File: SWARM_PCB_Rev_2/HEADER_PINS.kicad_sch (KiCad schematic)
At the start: 4 parts, among them J3 Conn_02x25_Odd_Even, J4 Conn_02x25_Odd_Even, J5 Conn_02x25_Odd_Even

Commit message: Reannotated Schematic
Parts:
- J1: renamed from J; value Conn_02x25_Odd_Even -> (none); footprint (none) -> SWARM_LIBRARY:HIROSE_DF40C-50DP-0.4V_51_; now left out of the parts list
- J2: renamed from J3; footprint (none) -> SWARM_LIBRARY:HIROSE_DF40C-50DP-0.4V_51_
- J3: renamed from J5; footprint (none) -> SWARM_LIBRARY:HIROSE_DF40C-50DP-0.4V_51_
- J4: footprint (none) -> SWARM_LIBRARY:HIROSE_DF40C-50DP-0.4V_51_
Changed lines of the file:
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@@
 		(body_style 1)
 		(exclude_from_sim no)
-		(in_bom yes)
+		(in_bom no)
 		(on_board yes)
 		(in_pos_files yes)
 		(dnp no)
-		(property "Reference" "J"
+		(property "Reference" "J1"
 			(at 38.1 25.4 0)
 			(show_name no)
@@
 			)
 		)
-		(property "Value" "Conn_02x25_Odd_Even"
+		(property "Value" ""
 			(at 38.1 24.13 0)
 			(hide yes)
@@
 			)
 		)
-		(property "Footprint" ""
+		(property "Footprint" "SWARM_LIBRARY:HIROSE_DF40C-50DP-0.4V_51_"
 			(at 36.83 58.42 0)
 			(hide yes)
@@
 		(pin "50"
 		)
-		(instances)
+		(instances
+			(project "SWARM_PCB_Rev_2"
+				(path "/d61c6b76-225f-4e7b-954b-419fd350b2a8/0ec9a5b8-e6af-498c-b79e-09f97163fe47/670af698-21c8-4937-8411-03789db7e644"
+					(reference "J1")
+					(unit 1)
+				)
+				(path "/d61c6b76-225f-4e7b-954b-419fd350b2a8/650025eb-067f-40e3-8b03-3f7becff6fc6/a42f8ac8-cc52-4f3b-92dd-c989c8ae3b1f"
+					(reference "J5")
+					(unit 1)
+				)
+				(path "/d61c6b76-225f-4e7b-954b-419fd350b2a8/eb158cd5-dda4-4d5d-aa38-aff400388cd2/b1c6b7e5-51b4-4fee-a7e7-18155b2b4cfe"
+					(reference "J9")
+					(unit 1)
+				)
+			)
+		)
 	)
 	(symbol
@@
 			)
 		)
-		(property "Footprint" ""
+		(property "Footprint" "SWARM_LIBRARY:HIROSE_DF40C-50DP-0.4V_51_"
 			(at 111.76 58.42 0)
 			(hide yes)
@@
 				(path "/d61c6b76-225f-4e7b-954b-419fd350b2a8/0ec9a5b8-e6af-498c-b79e-09f97163fe47/670af698-21c8-4937-8411-03789db7e644"
 					(reference "J4")
+					(unit 1)
+				)
+				(path "/d61c6b76-225f-4e7b-954b-419fd350b2a8/650025eb-067f-40e3-8b03-3f7becff6fc6/a42f8ac8-cc52-4f3b-92dd-c989c8ae3b1f"
+					(reference "J8")
+					(unit 1)
+				)
+				(path "/d61c6b76-225f-4e7b-954b-419fd350b2a8/eb158cd5-dda4-4d5d-aa38-aff400388cd2/b1c6b7e5-51b4-4fee-a7e7-18155b2b4cfe"
+					(reference "J12")
 					(unit 1)
 				)
@@
 		(in_pos_files yes)
 		(dnp no)
-		(property "Reference" "J5"
+		(property "Reference" "J3"
 			(at 95.25 25.4 0)
 			(show_name no)
@@
 			)
 		)
-		(property "Footprint" ""
+		(property "Footprint" "SWARM_LIBRARY:HIROSE_DF40C-50DP-0.4V_51_"
 			(at 96.52 58.42 0)
 			(hide yes)
@@
 			(project "SWARM_PCB_Rev_2"
 				(path "/d61c6b76-225f-4e7b-954b-419fd350b2a8/0ec9a5b8-e6af-498c-b79e-09f97163fe47/670af698-21c8-4937-8411-03789db7e644"
-					(reference "J5")
+					(reference "J3")
+					(unit 1)
+				)
+				(path "/d61c6b76-225f-4e7b-954b-419fd350b2a8/650025eb-067f-40e3-8b03-3f7becff6fc6/a42f8ac8-cc52-4f3b-92dd-c989c8ae3b1f"
+					(reference "J7")
+					(unit 1)
+				)
+				(path "/d61c6b76-225f-4e7b-954b-419fd350b2a8/eb158cd5-dda4-4d5d-aa38-aff400388cd2/b1c6b7e5-51b4-4fee-a7e7-18155b2b4cfe"
+					(reference "J11")
 					(unit 1)
 				)
@@
 		(in_pos_files yes)
 		(dnp no)
-		(property "Reference" "J3"
+		(property "Reference" "J2"
 			(at 53.34 25.4 0)
 			(show_name no)
@@
 			)
 		)
-		(property "Footprint" ""
+		(property "Footprint" "SWARM_LIBRARY:HIROSE_DF40C-50DP-0.4V_51_"
 			(at 52.07 58.42 0)
 			(hide yes)
@@
 			(project "SWARM_PCB_Rev_2"
 				(path "/d61c6b76-225f-4e7b-954b-419fd350b2a8/0ec9a5b8-e6af-498c-b79e-09f97163fe47/670af698-21c8-4937-8411-03789db7e644"
-					(reference "J3")
-					(unit 1)
-				)
+					(reference "J2")
+					(unit 1)
+				)
+				(path "/d61c6b76-225f-4e7b-954b-419fd350b2a8/650025eb-067f-40e3-8b03-3f7becff6fc6/a42f8ac8-cc52-4f3b-92dd-c989c8ae3b1f"
+					(reference "J6")
+					(unit 1)
+				)
+				(path "/d61c6b76-225f-4e7b-954b-419fd350b2a8/eb158cd5-dda4-4d5d-aa38-aff400388cd2/b1c6b7e5-51b4-4fee-a7e7-18155b2b4cfe"
+					(reference "J10")
+					(unit 1)
+				)

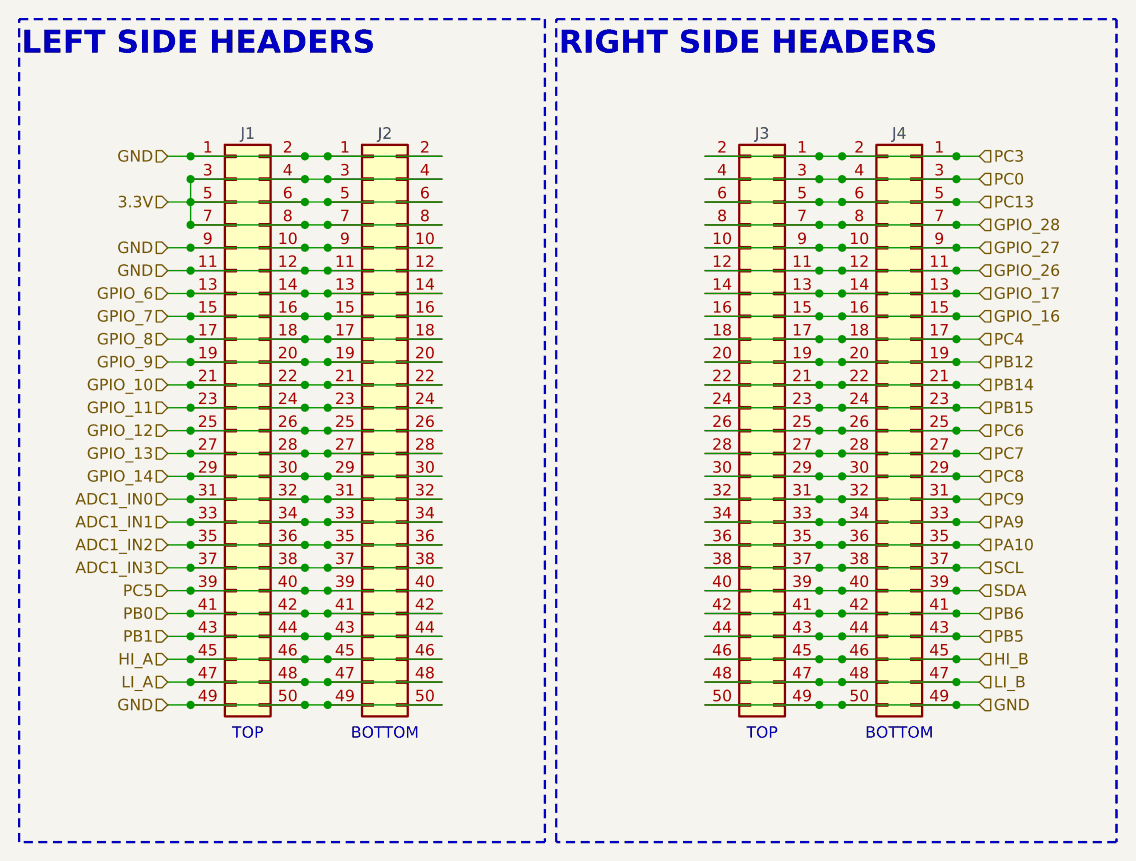
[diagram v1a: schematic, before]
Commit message: Finished Placement for POWER, CONTROL and SENSOR
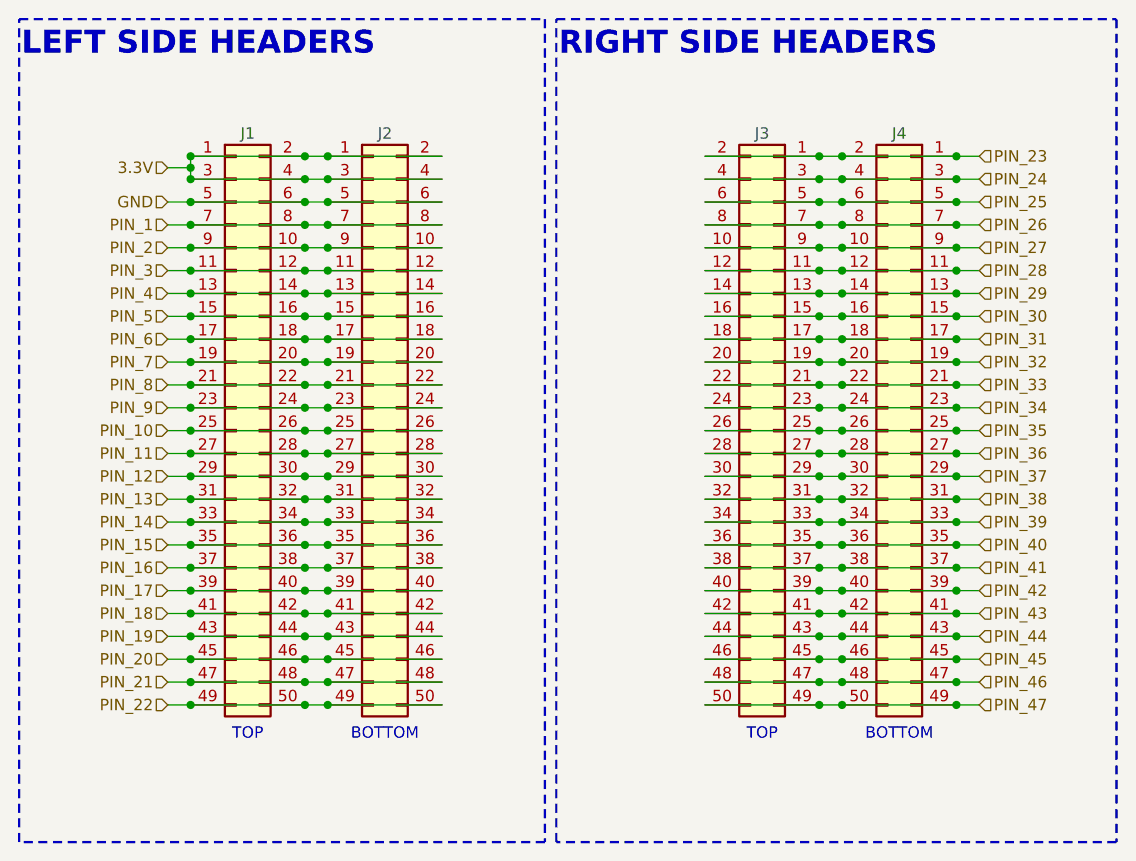
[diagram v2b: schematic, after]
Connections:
- net 3.3V: now also J1.1 (Pin_1), J1.2 (Pin_2), J2.1 (Pin_1), J2.2 (Pin_2); no longer J1.5 (Pin_5), J1.6 (Pin_6), J1.7 (Pin_7), J1.8 (Pin_8), J2.5 (Pin_5), J2.6 (Pin_6), J2.7 (Pin_7), J2.8 (Pin_8)
- net GND: now also J1.5 (Pin_5), J1.6 (Pin_6), J2.5 (Pin_5), J2.6 (Pin_6); no longer J1.1 (Pin_1), J1.10 (Pin_10), J1.11 (Pin_11), J1.12 (Pin_12), J1.2 (Pin_2), J1.49 (Pin_49), J1.50 (Pin_50), J1.9 (Pin_9), J2.1 (Pin_1), J2.10 (Pin_10), J2.11 (Pin_11), J2.12 (Pin_12), J2.2 (Pin_2), J2.49 (Pin_49), J2.50 (Pin_50), J2.9 (Pin_9), J3.49 (Pin_49), J3.50 (Pin_50), J4.49 (Pin_49), J4.50 (Pin_50)
- net ADC1_IN0 renamed PIN_13
- net ADC1_IN1 renamed PIN_14
- net ADC1_IN2 renamed PIN_15
- net ADC1_IN3 renamed PIN_16
- net GPIO_10 renamed PIN_8
- net GPIO_11 renamed PIN_9
- net GPIO_12 renamed PIN_10
- net GPIO_13 renamed PIN_11
- net GPIO_14 renamed PIN_12
- net GPIO_16 renamed PIN_30
- net GPIO_17 renamed PIN_29
- net GPIO_26 renamed PIN_28
- net GPIO_27 renamed PIN_27
- net GPIO_28 renamed PIN_26
- net GPIO_6 renamed PIN_4
- net GPIO_7 renamed PIN_5
- net GPIO_8 renamed PIN_6
- net GPIO_9 renamed PIN_7
- net HI_A renamed PIN_20
- net HI_B renamed PIN_45
- net LI_A renamed PIN_21
- net LI_B renamed PIN_46
- net PA10 renamed PIN_40
- net PA9 renamed PIN_39
- net PB0 renamed PIN_18
- net PB1 renamed PIN_19
- net PB12 renamed PIN_32
- net PB14 renamed PIN_33
- net PB15 renamed PIN_34
- net PB5 renamed PIN_44
- net PB6 renamed PIN_43
- net PC0 renamed PIN_24
- net PC13 renamed PIN_25
- net PC3 renamed PIN_23
- net PC4 renamed PIN_31
- net PC5 renamed PIN_17
- net PC6 renamed PIN_35
- net PC7 renamed PIN_36
- net PC8 renamed PIN_37
- net PC9 renamed PIN_38
- net SCL renamed PIN_41
- net SDA renamed PIN_42
- new net PIN_1: J1.7 (Pin_7), J1.8 (Pin_8), J2.7 (Pin_7), J2.8 (Pin_8)
- new net PIN_2: J1.10 (Pin_10), J1.9 (Pin_9), J2.10 (Pin_10), J2.9 (Pin_9)
- new net PIN_22: J1.49 (Pin_49), J1.50 (Pin_50), J2.49 (Pin_49), J2.50 (Pin_50)
- new net PIN_3: J1.11 (Pin_11), J1.12 (Pin_12), J2.11 (Pin_11), J2.12 (Pin_12)
- new net PIN_47: J3.49 (Pin_49), J3.50 (Pin_50), J4.49 (Pin_49), J4.50 (Pin_50)
